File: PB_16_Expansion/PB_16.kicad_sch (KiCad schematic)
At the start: 25 parts, among them J1 USB, J2 OLED Conn, J3 GPIO Header, J4 RTC Conn, J5 Power In, J6 VIN_Voltage, J7 Output Header, J8 Output Header, J9 Serial Out, SW1 OLED Select, SW4 Enter BTN, SW5 Down BTN, U1 Universe5V, U4 24LC256

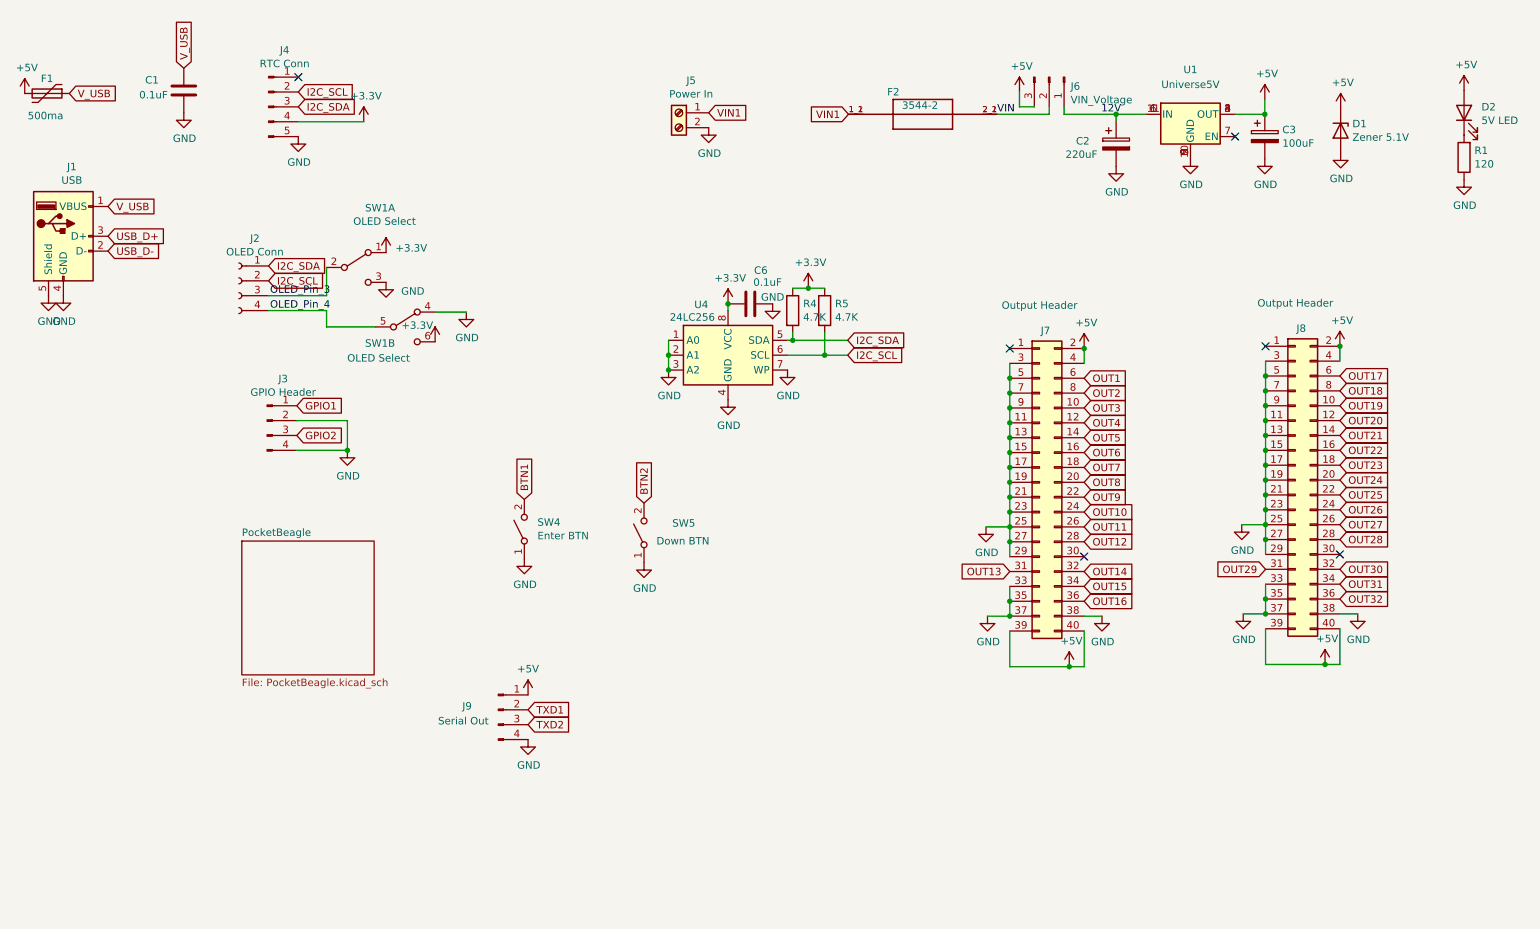
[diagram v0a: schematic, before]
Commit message: PB_16_Expansion v5 ---- * 2026-02-20 * Add Different Output * Switched Expansion Header to 24pin Falcon V4 pinout. * Switched to PB16v2 pinout, use PB16v2 EEPROM
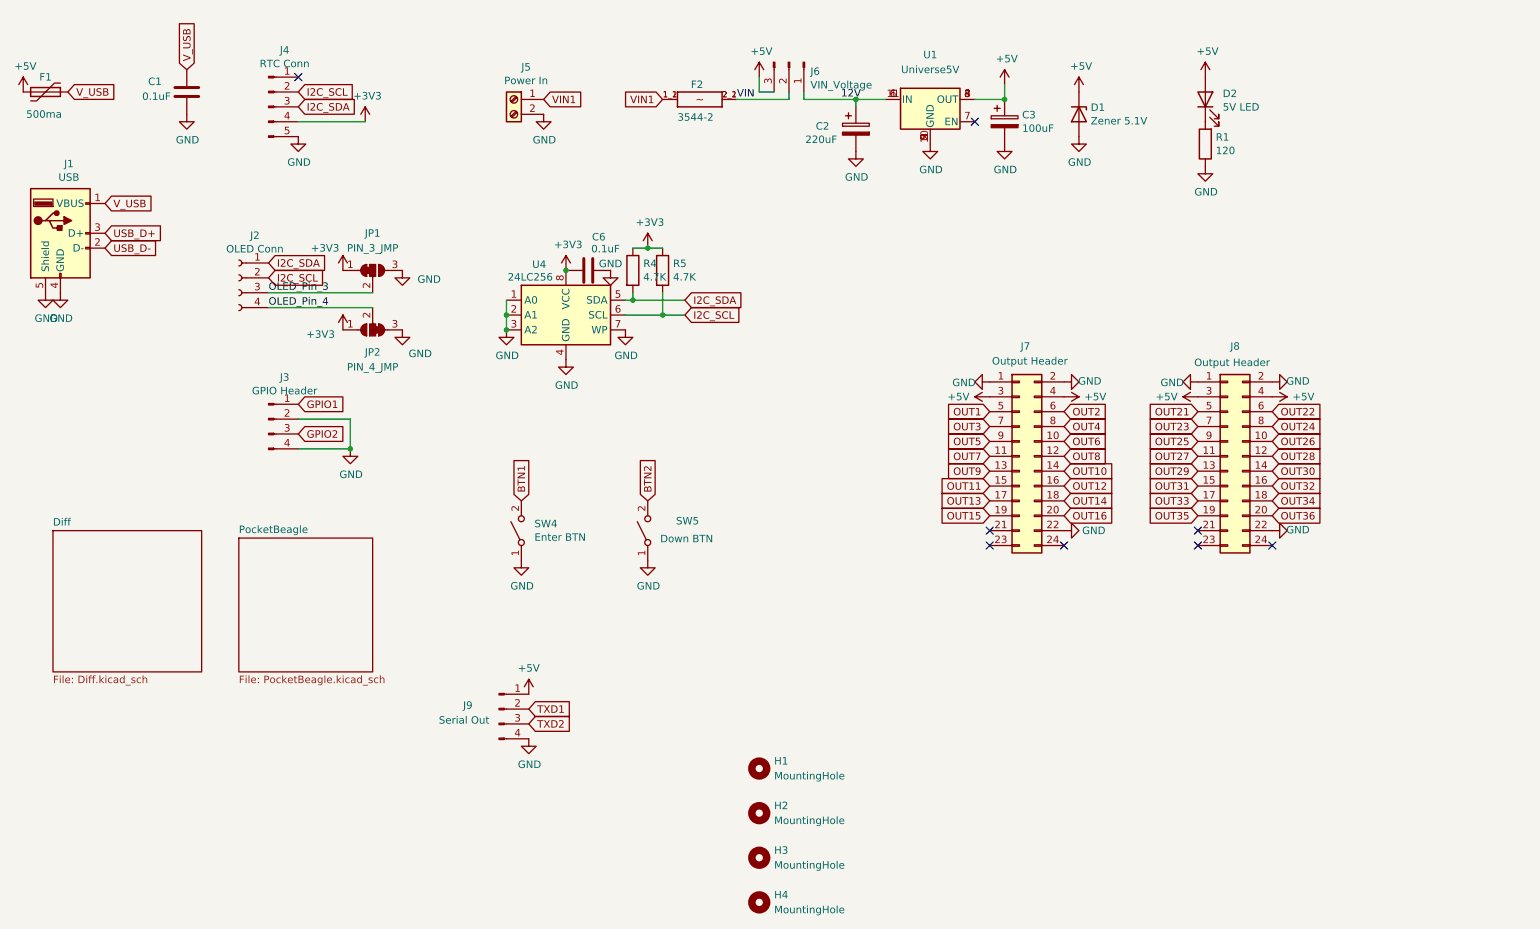
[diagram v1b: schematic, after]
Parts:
- removed SW1: OLED Select, Button_Switch_THT:SW_CuK_JS202011CQN_DPDT_Straight, symbol Switch:SW_DPDT_x2
- added H1, H2, H3, H4: MountingHole, Scotts:MountingHole_3.7mm, symbol Mechanical:MountingHole
- added JP1: PIN_3_JMP, Scotts:SolderJumper-3_P1mm_Bridged12, symbol Scotts:SolderJumper_3_Bridged12
- added JP2: PIN_4_JMP, Scotts:SolderJumper-3_P1mm_Bridged23, symbol Scotts:SolderJumper_3_Bridged23
- F2: footprint Keystone_Fuse:FUSE_3544-2 -> Scotts:FUSE_3544-2; symbol PB_16-rescue:3544-2-Keystone_Fuse -> Scotts:3544-2; LCSC (none) -> C492610
- J7, J8: footprint Connector_IDC:IDC-Header_2x20_P2.54mm_Vertical -> Connector_IDC:IDC-Header_2x12_P2.54mm_Vertical; symbol Connector_Generic:Conn_02x20_Odd_Even -> Connector_Generic:Conn_02x12_Odd_Even; Digi-Key_PN S9175-ND -> 732-5398-ND; MPN SBH11-PBPC-D20-ST-BK -> 61202421621
- U1: Digi-Key_PN (none) -> 811-2692-ND; MPN (none) -> OKI-78SR-5/1.5-W36H-C
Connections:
- net OUT17 is gone; now on net OUT22: J8.6 (Pin_6)
- net OUT18 is gone; now on net OUT24: J8.8 (Pin_8)
- net OUT19 is gone; now on net OUT26: J8.10 (Pin_10)
- net OUT20 is gone; now on net OUT28: J8.12 (Pin_12)
- net +3V3: now also JP1.1 (A), JP2.1 (A)
- net +5V: now also J7.3 (Pin_3), J8.3 (Pin_3); no longer J7.2 (Pin_2), J7.39 (Pin_39), J7.40 (Pin_40), J8.2 (Pin_2), J8.39 (Pin_39), J8.40 (Pin_40)
- net GND: now also J7.1 (Pin_1), J7.2 (Pin_2), J7.22 (Pin_22), J8.1 (Pin_1), J8.2 (Pin_2), J8.22 (Pin_22), JP1.3 (B), JP2.3 (B); no longer J7.11 (Pin_11), J7.13 (Pin_13), J7.15 (Pin_15), J7.17 (Pin_17), J7.19 (Pin_19), J7.21 (Pin_21), J7.23 (Pin_23), J7.25 (Pin_25), J7.27 (Pin_27), J7.29 (Pin_29), J7.3 (Pin_3), J7.33 (Pin_33), J7.35 (Pin_35), J7.37 (Pin_37), J7.38 (Pin_38), J7.5 (Pin_5), J7.7 (Pin_7), J7.9 (Pin_9), J8.11 (Pin_11), J8.13 (Pin_13), J8.15 (Pin_15), J8.17 (Pin_17), J8.19 (Pin_19), J8.21 (Pin_21), J8.23 (Pin_23), J8.25 (Pin_25), J8.27 (Pin_27), J8.29 (Pin_29), J8.3 (Pin_3), J8.33 (Pin_33), J8.35 (Pin_35), J8.37 (Pin_37), J8.38 (Pin_38), J8.5 (Pin_5), J8.7 (Pin_7), J8.9 (Pin_9)
- net OLED_Pin_3: now also JP1.2 (C)
- net OLED_Pin_4: now also JP2.2 (C)
- net OUT1: now also J7.5 (Pin_5); no longer J7.6 (Pin_6)
- net OUT10: now also J7.14 (Pin_14); no longer J7.24 (Pin_24)
- net OUT11: now also J7.15 (Pin_15); no longer J7.26 (Pin_26)
- net OUT12: now also J7.16 (Pin_16); no longer J7.28 (Pin_28)
- net OUT13: now also J7.17 (Pin_17); no longer J7.31 (Pin_31)
- net OUT14: now also J7.18 (Pin_18); no longer J7.32 (Pin_32)
- net OUT15: now also J7.19 (Pin_19); no longer J7.34 (Pin_34)
- net OUT16: now also J7.20 (Pin_20); no longer J7.36 (Pin_36)
- net OUT2: now also J7.6 (Pin_6); no longer J7.8 (Pin_8)
- net OUT21: now also J8.5 (Pin_5); no longer J8.14 (Pin_14)
- net OUT22: no longer J8.16 (Pin_16)
- net OUT23: now also J8.7 (Pin_7); no longer J8.18 (Pin_18)
- net OUT24: no longer J8.20 (Pin_20)
- net OUT25: now also J8.9 (Pin_9); no longer J8.22 (Pin_22)
- net OUT26: no longer J8.24 (Pin_24)
- net OUT27: now also J8.11 (Pin_11); no longer J8.26 (Pin_26)
- net OUT28: no longer J8.28 (Pin_28)
- net OUT29: now also J8.13 (Pin_13); no longer J8.31 (Pin_31)
- net OUT3: now also J7.7 (Pin_7); no longer J7.10 (Pin_10)
- net OUT30: now also J8.14 (Pin_14); no longer J8.32 (Pin_32)
- net OUT31: now also J8.15 (Pin_15); no longer J8.34 (Pin_34)
- net OUT32: now also J8.16 (Pin_16); no longer J8.36 (Pin_36)
- net OUT4: now also J7.8 (Pin_8); no longer J7.12 (Pin_12)
- net OUT5: now also J7.9 (Pin_9); no longer J7.14 (Pin_14)
- net OUT6: now also J7.10 (Pin_10); no longer J7.16 (Pin_16)
- net OUT7: now also J7.11 (Pin_11); no longer J7.18 (Pin_18)
- net OUT8: now also J7.12 (Pin_12); no longer J7.20 (Pin_20)
- net OUT9: now also J7.13 (Pin_13); no longer J7.22 (Pin_22)
- new net OUT33: J8.17 (Pin_17)
- new net OUT34: J8.18 (Pin_18)
- new net OUT35: J8.19 (Pin_19)
- new net OUT36: J8.20 (Pin_20)
- no-connect marks 6 -> 8
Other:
- added sheet Diff (Diff.kicad_sch)
- moved on the sheet: C1, C2, C3, C6, D1, D2, F2, J1, J2, J5, J6, R1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
